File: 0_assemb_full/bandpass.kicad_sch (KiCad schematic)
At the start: 29 parts, among them U15 X-opamp,IEEE, U16 X-opamp,IEEE, U17 X-opamp,IEEE, U18 X-opamp,IEEE, U19 X-opamp,IEEE, U20 X-opamp,IEEE, U21 X-opamp,IEEE, U22 X-opamp,IEEE

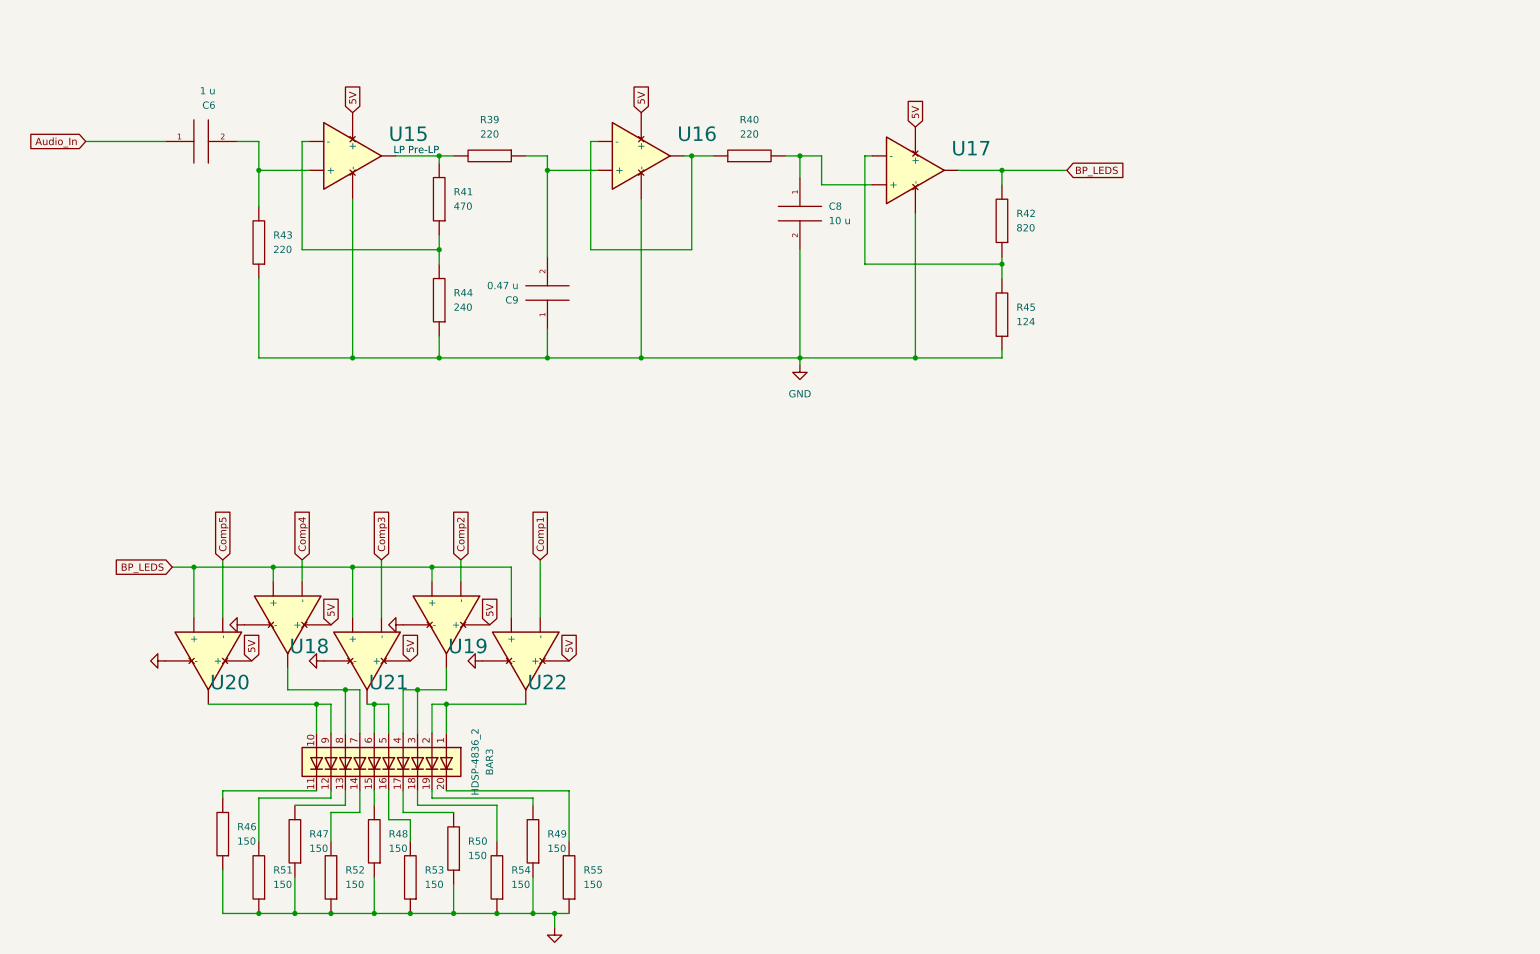
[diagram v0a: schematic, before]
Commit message: Added the full schematic file and included the filters
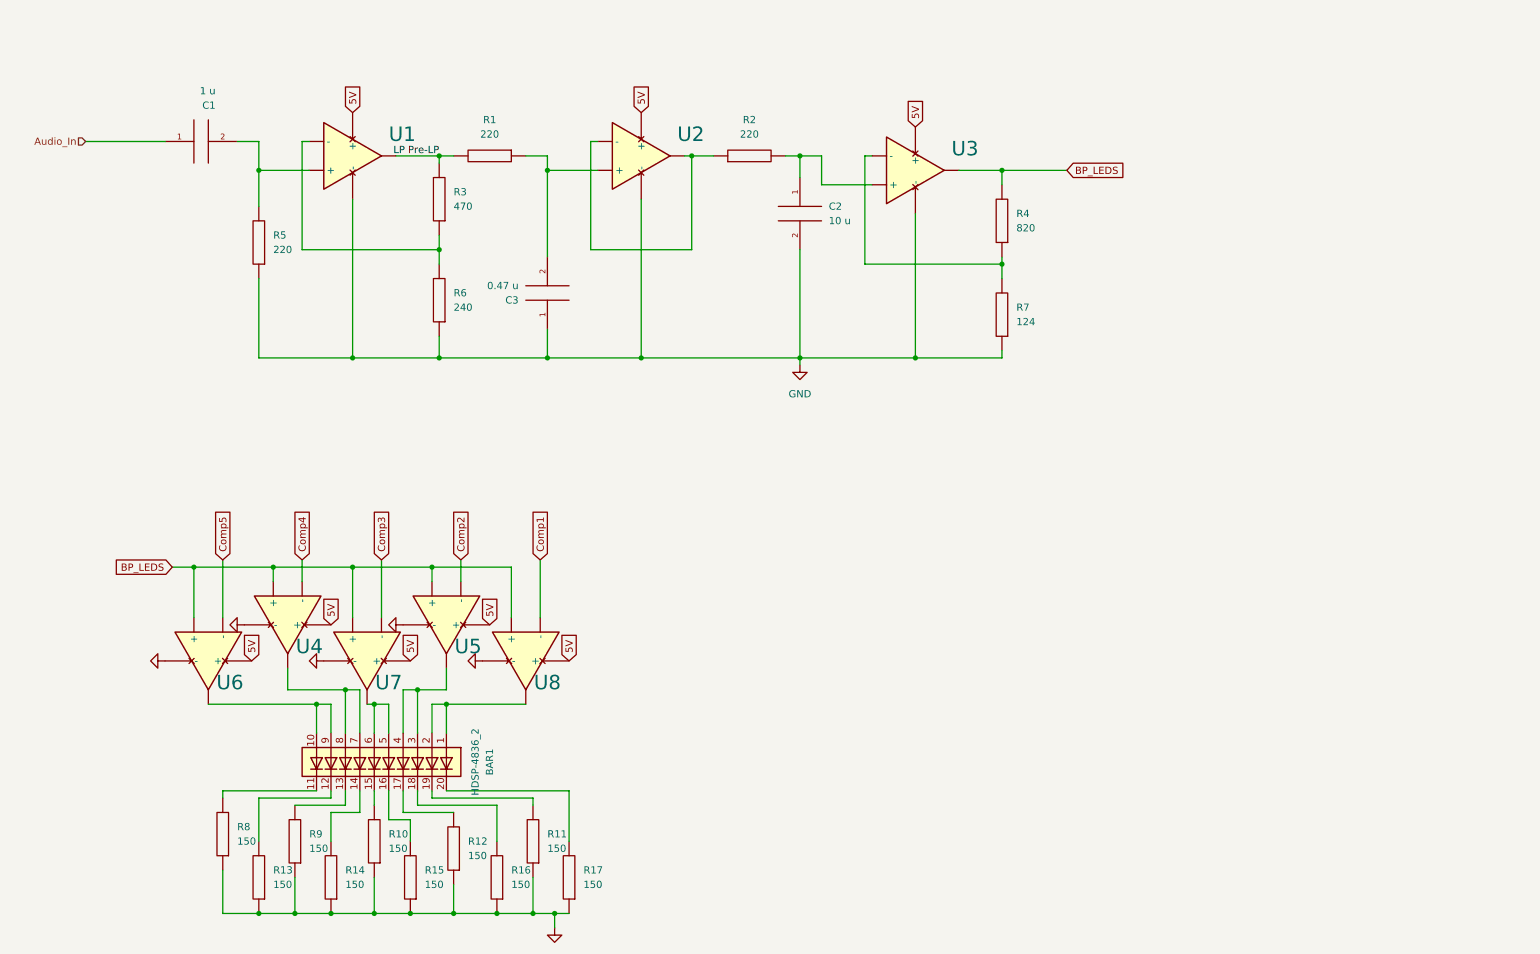
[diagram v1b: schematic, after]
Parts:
- renumbered BAR3 to BAR1, C6 to C1, C8 to C2, C9 to C3, R39 to R1, R48 to R10, R49 to R11, R50 to R12, R51 to R13, R52 to R14, R53 to R15, R54 to R16, R55 to R17, R40 to R2, R41 to R3, R42 to R4, R43 to R5, R44 to R6, R45 to R7, R46 to R8, R47 to R9, U15 to U1, U16 to U2, U17 to U3, U18 to U4, U19 to U5, U20 to U6, U21 to U7, U22 to U8

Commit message: Added STM32F091RCTx symbol and power symbols
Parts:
- added R10, R11, R12, R13, R14, R15, R8, R9: 220, symbol pspice:R
- renumbered R8 to R16, R9 to R17, R10 to R18, R11 to R19, R12 to R20, R13 to R21, R14 to R22, R15 to R23, R16 to R24, R17 to R25, U1 to U2, U2 to U3, U3 to U4, U4 to U5, U5 to U6, U6 to U7, U7 to U8, U8 to U9
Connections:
- net 5V: now also R13.2
- net Comp1: now also R11.2, R12.2
- net Comp2: now also R10.2, R11.1
- net Comp3: now also R10.1, R9.2
- net Comp4: now also R8.2, R9.1
- net Comp5: now also R14.2, R8.1
- net GND: now also R12.1
- new net: R13.1, R15.2
- new net: R14.1, R15.1
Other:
- note added: "Comparator Ref Voltages"

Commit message: Additional changes
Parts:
- added RV1, RV2, RV3: 1K, symbol Device:Varistor_US
- C3: renamed from C1; value 1 u -> 1u
- C4: renamed from C2; value 10 u -> 10u
- C5: renamed from C3; value 0.47 u -> 0.47u
- R1, R2, R5: value 220 -> 470; symbol pspice:R -> Device:R_US
- R10, R11, R12, R13, R14, R15, R16, R17, R18, R19, R20, R21, R22, R23, R24, R25, R3, R4, R6, R7, R8, R9: symbol pspice:R -> Device:R_US
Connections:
- net GND: now also RV3.2
- net LP Pre-LP: now also RV1.2
- net at C5.2, R1.1, U3.1 (+): now also RV1.1
- net at C3.2, R5.2, U2.1 (+): now also RV3.1
- net at R2.1, U3.2 (-), U3.5 (OUT): now also RV2.2
- net at C4.1, R2.2, U4.1 (+): now also RV2.1
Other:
- note added: "Ideal: 220 Ohms"

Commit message: Removed varistors, updated some STM32 connections
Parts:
- removed RV1, RV2, RV3: 1K, symbol Device:Varistor_US
- R1, R2, R5: value 470 -> 220
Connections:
- net BP_LEDS renamed ADC_BP
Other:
- note removed: "Ideal: 220 Ohms"
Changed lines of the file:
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@@
   (junction (at 100.33 184.15) (diameter 0) (color 0 0 0 0)
   )
-  (junction (at 109.22 50.8) (diameter 0) (color 0 0 0 0)
-  )
   (junction (at 78.74 147.32) (diameter 0) (color 0 0 0 0)
   )
@@
   (junction (at 58.42 184.15) (diameter 0) (color 0 0 0 0)
   )
-  (junction (at 58.42 86.36) (diameter 0) (color 0 0 0 0)
-  )
   (junction (at 74.93 123.19) (diameter 0) (color 0 0 0 0)
   )
@@
     (stroke (width 0) (type default) (color 0 0 0 0))
   )
-  (wire (pts (xy 134.62 40.64) (xy 134.62 50.8))
-    (stroke (width 0) (type default) (color 0 0 0 0))
-  )
   (wire (pts (xy 100.33 181.61) (xy 100.33 184.15))
     (stroke (width 0) (type default) (color 0 0 0 0))
@@
     (stroke (width 0) (type default) (color 0 0 0 0))
   )
-  (wire (pts (xy 48.26 53.34) (xy 58.42 53.34))
-    (stroke (width 0) (type default) (color 0 0 0 0))
-  )
   (wire (pts (xy 90.17 50.8) (xy 95.25 50.8))
     (stroke (width 0) (type default) (color 0 0 0 0))
@@
     (stroke (width 0) (type default) (color 0 0 0 0))
   )
-  (wire (pts (xy 102.87 40.64) (xy 109.22 40.64))
-    (stroke (width 0) (type default) (color 0 0 0 0))
-  )
   (wire (pts (xy 262.89 143.51) (xy 262.89 146.05))
     (stroke (width 0) (type default) (color 0 0 0 0))
@@
     (stroke (width 0) (type default) (color 0 0 0 0))
   )
-  (wire (pts (xy 95.25 40.64) (xy 90.17 40.64))
-    (stroke (width 0) (type default) (color 0 0 0 0))
-  )
-  (wire (pts (xy 90.17 40.64) (xy 90.17 50.8))
-    (stroke (width 0) (type default) (color 0 0 0 0))
-  )
   (wire (pts (xy 109.22 50.8) (xy 109.22 53.34))
     (stroke (width 0) (type default) (color 0 0 0 0))
@@
     (stroke (width 0) (type default) (color 0 0 0 0))
   )
-  (wire (pts (xy 148.59 40.64) (xy 153.67 40.64))
-    (stroke (width 0) (type default) (color 0 0 0 0))
-  )
   (wire (pts (xy 86.36 165.1) (xy 86.36 162.56))
     (stroke (width 0) (type default) (color 0 0 0 0))
@@
     (stroke (width 0) (type default) (color 0 0 0 0))
   )
-  (wire (pts (xy 109.22 40.64) (xy 109.22 50.8))
-    (stroke (width 0) (type default) (color 0 0 0 0))
-  )
   (wire (pts (xy 217.17 143.51) (xy 220.98 143.51))
     (stroke (width 0) (type default) (color 0 0 0 0))
@@
     (stroke (width 0) (type default) (color 0 0 0 0))
   )
-  (wire (pts (xy 153.67 40.64) (xy 153.67 50.8))
-    (stroke (width 0) (type default) (color 0 0 0 0))
-  )
-  (wire (pts (xy 48.26 53.34) (xy 48.26 66.04))
-    (stroke (width 0) (type default) (color 0 0 0 0))
-  )
   (wire (pts (xy 63.5 144.78) (xy 73.66 144.78))
     (stroke (width 0) (type default) (color 0 0 0 0))
@@
     (stroke (width 0) (type default) (color 0 0 0 0))
   )
-  (wire (pts (xy 140.97 40.64) (xy 134.62 40.64))
-    (stroke (width 0) (type default) (color 0 0 0 0))
-  )
   (wire (pts (xy 66.04 121.92) (xy 66.04 125.73))
     (stroke (width 0) (type default) (color 0 0 0 0))
@@
     (stroke (width 0) (type default) (color 0 0 0 0))
   )
-  (wire (pts (xy 48.26 73.66) (xy 48.26 86.36))
-    (stroke (width 0) (type default) (color 0 0 0 0))
-  )
   (wire (pts (xy 90.17 80.01) (xy 90.17 86.36))
     (stroke (width 0) (type default) (color 0 0 0 0))
@@
     (stroke (width 0) (type default) (color 0 0 0 0))
   )
-  (wire (pts (xy 48.26 86.36) (xy 58.42 86.36))
-    (stroke (width 0) (type default) (color 0 0 0 0))
-  )
   (wire (pts (xy 153.67 86.36) (xy 173.99 86.36))
     (stroke (width 0) (type default) (color 0 0 0 0))
-  )
-  (text "Ideal:\n220 Ohms" (at 38.1 57.15 0)
-    (effects (font (size 1.27 1.27)) (justify left bottom))
-  )
-  (text "Ideal:\n220 Ohms" (at 129.54 40.64 0)
-    (effects (font (size 1.27 1.27)) (justify left bottom))
-  )
-  (text "Ideal:\n220 Ohms" (at 85.09 40.64 0)
-    (effects (font (size 1.27 1.27)) (justify left bottom))
   )
   (text "Comparator Ref Voltages" (at 175.26 133.35 0)
@@
     (effects (font (size 1.27 1.27)) (justify left))
     (property "Intersheet References" "${INTERSHEET_REFS}" (id 0) (at 85.0106 134.9888 90)
+      (effects (font (size 1.27 1.27)) (justify left) hide)
+    )
+  )
+  (global_label "ADC_BP" (shape input) (at 200.66 53.34 0) (fields_autoplaced)
+    (effects (font (size 1.27 1.27)) (justify left))
+    (property "Intersheet References" "${INTERSHEET_REFS}" (id 0) (at 210.2093 53.2606 0)
       (effects (font (size 1.27 1.27)) (justify left) hide)
     )
@@
     (pin "2")
   )
-  (symbol (lib_id "Device:Varistor_US") (at 48.26 69.85 0) (unit 1)
-    (in_bom yes) (on_board yes) (fields_autoplaced)
-    (property "Reference" "RV3" (id 0) (at 50.8 68.8966 0)
-      (effects (font (size 1.27 1.27)) (justify left))
-    )
-    (property "Value" "1K" (id 1) (at 50.8 71.4366 0)
-      (effects (font (size 1.27 1.27)) (justify left))
-    )
-    (property "Footprint" "" (id 2) (at 46.482 69.85 90)
-      (effects (font (size 1.27 1.27)) hide)
-    )
-    (property "Datasheet" "~" (id 3) (at 48.26 69.85 0)
-      (effects (font (size 1.27 1.27)) hide)
-    )
-    (pin "1")
-    (pin "2")
-  )
   (symbol (lib_id "power:GND") (at 41.91 139.7 270) (unit 1)
     (in_bom yes) (on_board yes) (fields_autoplaced)
@@
     (in_bom yes) (on_board yes) (fields_autoplaced)
     (property "Reference" "R1" (id 0) (at 99.06 44.45 90))
-    (property "Value" "470" (id 1) (at 99.06 46.99 90))
+    (property "Value" "220" (id 1) (at 99.06 46.99 90))
     (property "Footprint" "" (id 2) (at 98.806 51.816 90)
       (effects (font (size 1.27 1.27)) hide)
@@
       (effects (font (size 1.27 1.27)) (justify right))
     )
-    (property "Value" "470" (id 1) (at 60.96 71.1199 0)
+    (property "Value" "220" (id 1) (at 60.96 71.1199 0)
       (effects (font (size 1.27 1.27)) (justify right))
     )
@@
     (pin "5")
   )
-  (symbol (lib_id "Device:Varistor_US") (at 99.06 40.64 270) (unit 1)
-    (in_bom yes) (on_board yes) (fields_autoplaced)
-    (property "Reference" "RV1" (id 0) (at 98.7433 33.02 90))
-    (property "Value" "1K" (id 1) (at 98.7433 35.56 90))
-    (property "Footprint" "" (id 2) (at 99.06 38.862 90)
-      (effects (font (size 1.27 1.27)) hide)
-    )
-    (property "Datasheet" "~" (id 3) (at 99.06 40.64 0)
-      (effects (font (size 1.27 1.27)) hide)
-    )
-    (pin "1")
-    (pin "2")
-  )
   (symbol (lib_id "pspice:C") (at 109.22 74.93 180) (unit 1)
     (in_bom yes) (on_board yes)
@@
     (in_bom yes) (on_board yes) (fields_autoplaced)
     (property "Reference" "R2" (id 0) (at 144.78 44.45 90))
-    (property "Value" "470" (id 1) (at 144.78 46.99 90))
+    (property "Value" "220" (id 1) (at 144.78 46.99 90))
     (property "Footprint" "" (id 2) (at 145.034 49.784 90)
       (effects (font (size 1.27 1.27)) hide)
@@
     (pin "5")
   )
-  (symbol (lib_id "Device:Varistor_US") (at 144.78 40.64 270) (unit 1)
-    (in_bom yes) (on_board yes) (fields_autoplaced)
-    (property "Reference" "RV2" (id 0) (at 144.4633 33.02 90))
-    (property "Value" "1K" (id 1) (at 144.4633 35.56 90))
-    (property "Footprint" "" (id 2) (at 144.78 38.862 90)
-      (effects (font (size 1.27 1.27)) hide)
-    )
-    (property "Datasheet" "~" (id 3) (at 144.78 40.64 0)
-      (effects (font (size 1.27 1.27)) hide)
-    )
-    (pin "1")
-    (pin "2")
-  )
   (symbol (lib_id "Generic:X-opamp,IEEE") (at 74.93 50.8 0) (unit 1)

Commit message: Bandpass filter all set now!
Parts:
- removed C4: 10u, symbol pspice:C
- removed R2: 220, symbol Device:R_US
- added C3, C5: 1u, symbol pspice:C
- added C6: 10u, symbol pspice:C
- added R1, R4: 240, symbol Device:R_US
- added R10: 56K, symbol Device:R_US
- added R3: 1K, symbol Device:R_US
- added R6: 33K, symbol Device:R_US
- added U5: X-opamp,IEEE, symbol Generic:X-opamp,IEEE
- C7: renamed from C5; value 0.47u -> 1u
- R2: renamed from R1; value 220 -> 1K
- R5: renamed from R3; value 470 -> 33K
- R7: renamed from R4; value 820 -> 560
- R8: renamed from R5; value 220 -> 240
- R9: renamed from R6; value 240 -> 56K
- renumbered C3 to C4, R7 to R11, R8 to R12, R9 to R13, R10 to R14, R11 to R15, R12 to R16, R13 to R17, R14 to R18, R15 to R19, R16 to R20, R17 to R21, R18 to R22, R19 to R23, R20 to R24, R21 to R25, R22 to R26, R23 to R27, R24 to R28, R25 to R29, U9 to U10, U5 to U6, U6 to U7, U7 to U8, U8 to U9
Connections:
- net 5V: now also U5.3 (+)
- net ADC_BP: now also U5.2 (-), U5.5 (OUT); no longer R7.2, U4.5 (OUT)
- net GND: now also C6.2, R10.1, U5.4 (-)
- net LP Pre-LP: now also R1.1
- net at C7.2, U3.1 (+): now also R3.1; no longer R2.1
- net at R8.2, U2.1 (+): now also C5.2; no longer C4.2
- net at U3.2 (-): now also R10.2, R6.1; no longer U3.5 (OUT)
- net at U4.1 (+): now also U3.5 (OUT), C3.1, R6.2
- new net: C3.2, R2.1, R3.2
- new net: C4.2, C5.1, R1.2
- new net: C6.1, R4.2, U5.1 (+)
- new net: R4.1, R7.2, U4.5 (OUT)
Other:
- moved on the sheet: C4, C7, R11, R2, R7, R8, U3, U4

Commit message: A bunch of changes to the schematics
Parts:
- removed BAR1: HDSP-4836_2, Display:HDSP-4836, symbol LED:HDSP-4836_2
- removed R20, R21, R22, R23, R24, R25, R26, R27, R28, R29: 150, symbol Device:R_US
- removed U10, U6, U7, U8, U9: X-opamp,IEEE, symbol Generic:X-opamp,IEEE

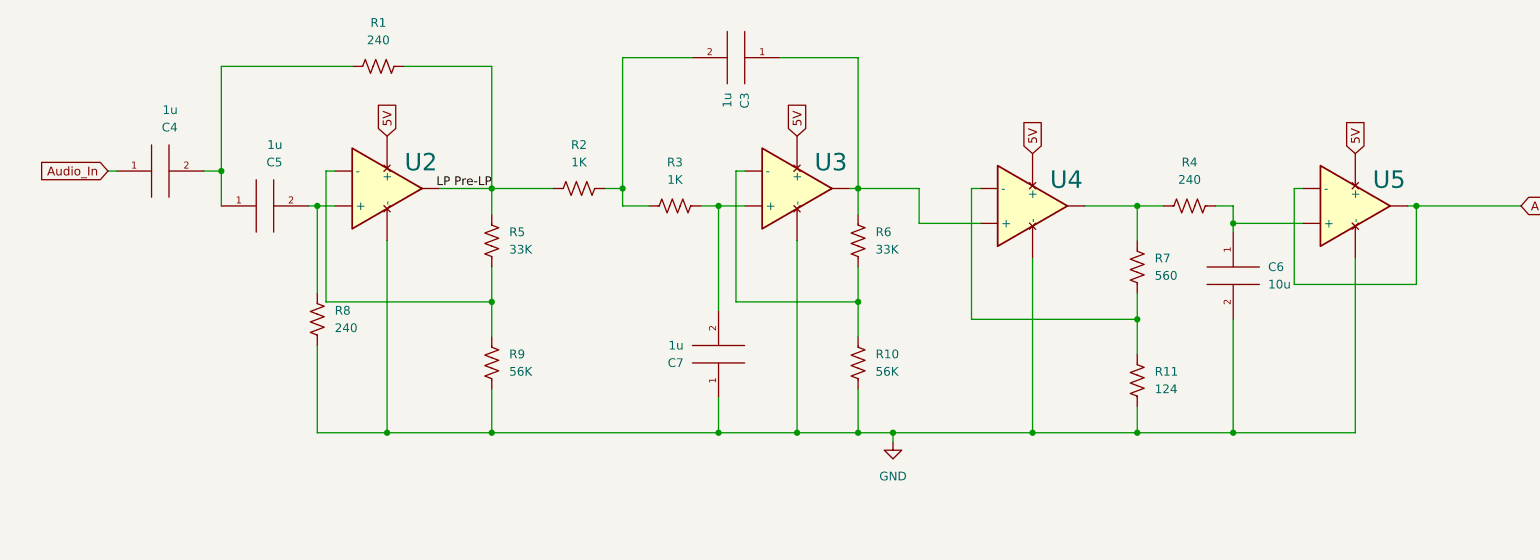
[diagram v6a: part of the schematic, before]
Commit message: Updates to the filter system
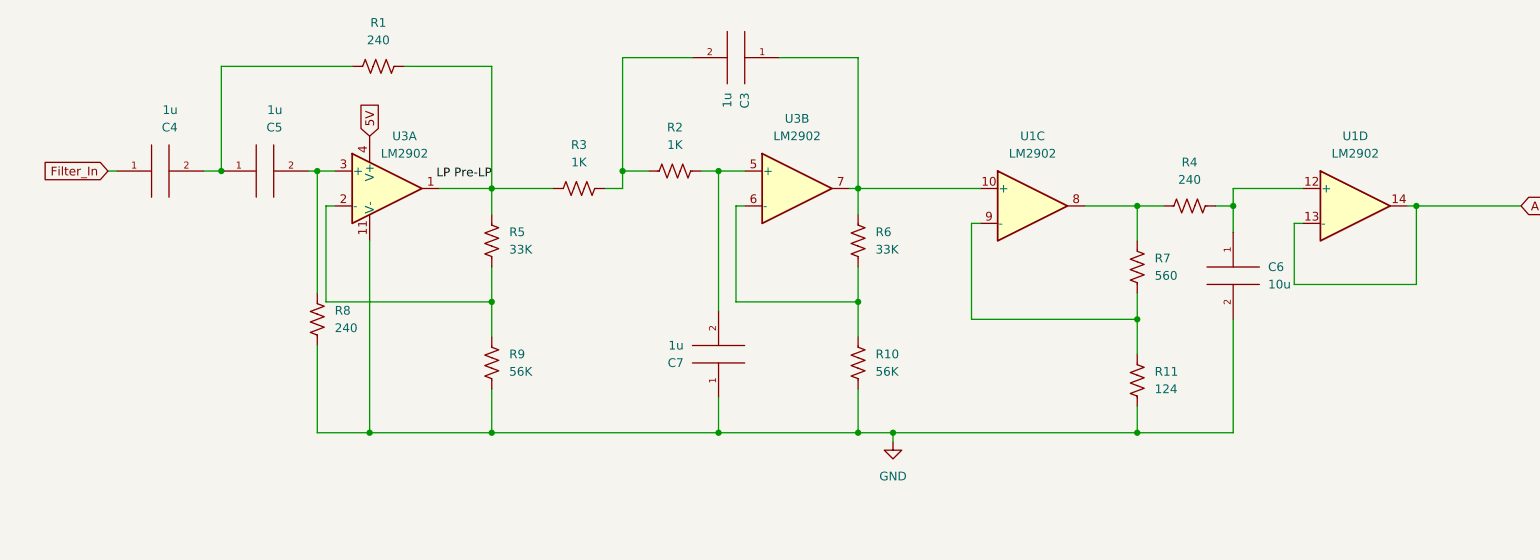
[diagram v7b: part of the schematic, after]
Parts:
- removed U2, U3, U4, U5: X-opamp,IEEE, symbol Generic:X-opamp,IEEE
- added U1, U3: LM2902, symbol Amplifier_Operational:LM2902
- renumbered R3 to R2, R2 to R3
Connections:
- net 5V: now also U3.4 (V+)
- net ADC_BP: now also U1.13 (-), U1.14
- net GND: now also U3.11 (V-)
- net LP Pre-LP: now also U3.1
- net at R5.1, R9.2: now also U3.2 (-)
- net at R10.2, R6.1: now also U3.6 (-)
- net at C3.1, R6.2: now also U1.10 (+), U3.7
- net at C5.2, R8.2: now also U3.3 (+)
- net at C6.1, R4.2: now also U1.12 (+)
- net at R11.2, R7.1: now also U1.9 (-)
- net at R4.1, R7.2: now also U1.8
- net at C7.2, R2.1: now also U3.5 (+)
- net Audio_In renamed Filter_In
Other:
- moved on the sheet: C5, R2
